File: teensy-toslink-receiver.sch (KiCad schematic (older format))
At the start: 11 parts, among them J1 Conn_01x03, J2 Conn_01x05, J3 Conn_01x05, J4 Conn_01x05, J5 Conn_01x03, J6 Conn_01x04, J7 HDMI_A_1.4, U1 PLR135-T10

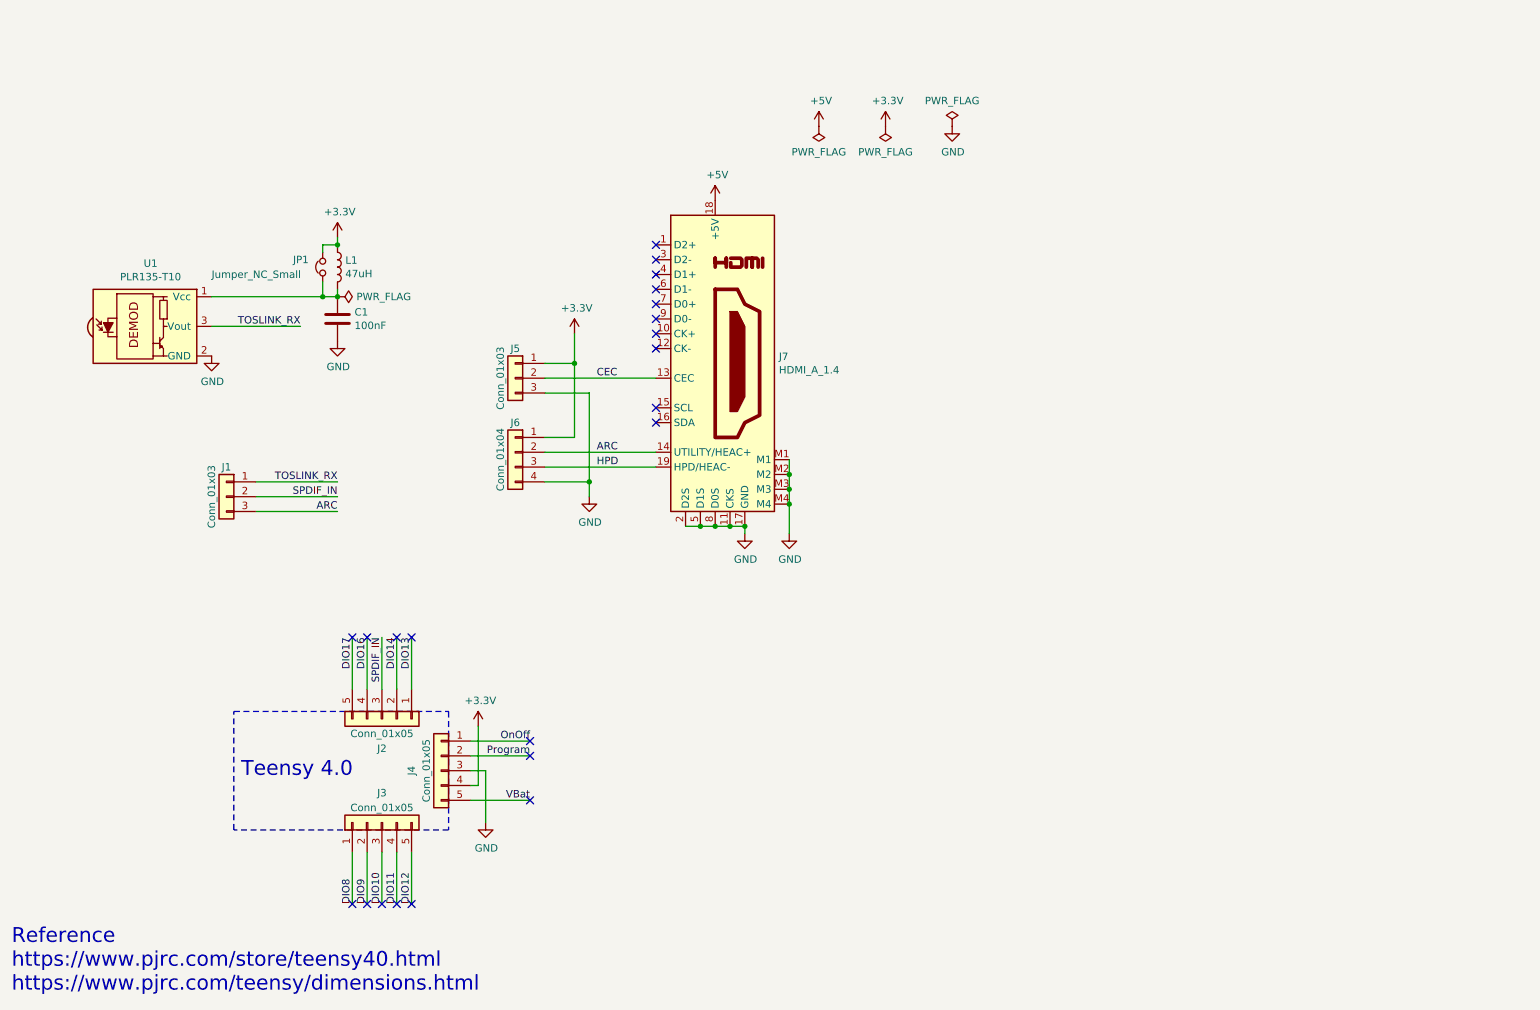
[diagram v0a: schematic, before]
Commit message: schematic: Add HPD and CEC FETs
* N-Channel MOSFET to pull HPD low on connection.
* N-Channel MOSFET acting as a diode to prevent dragging bus down.
* N-Channel MOSFET to detect when HDMI cable is plugged in and 5V is
  available to start operation.
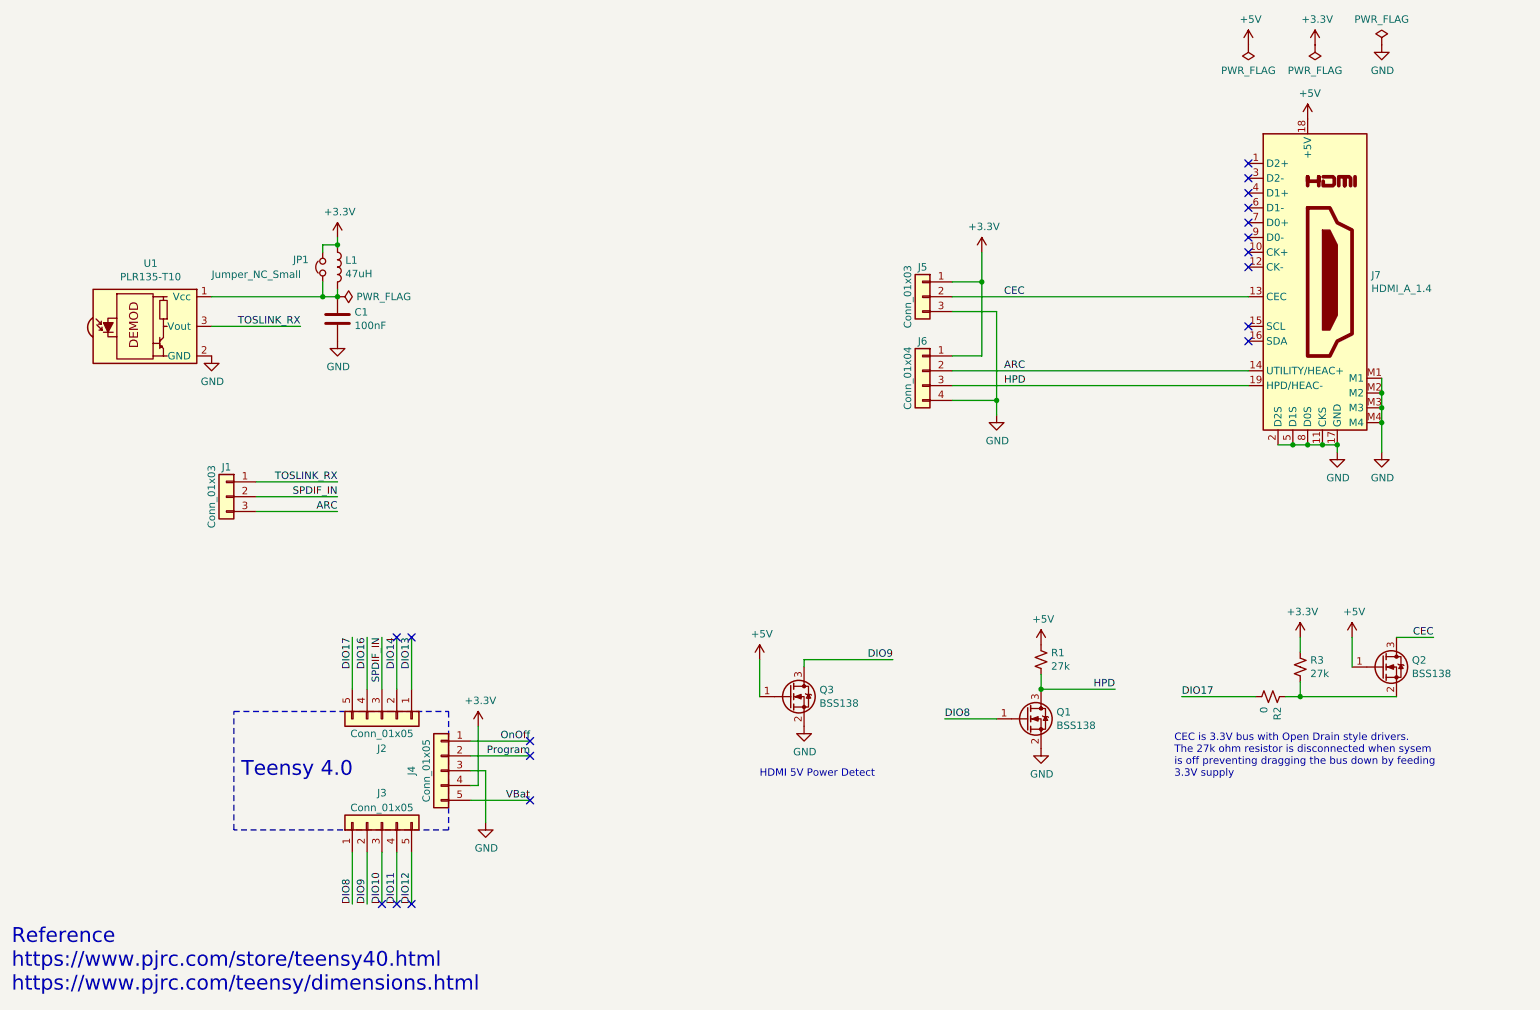
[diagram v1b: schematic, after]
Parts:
- added Q1, Q2, Q3: BSS138, Package_TO_SOT_SMD:SOT-23, symbol Transistor_FET:BSS138
- added R1, R3: 27k, Resistor_SMD:R_0201_0603Metric, symbol Device:R_Small_US
- added R2: 0, Resistor_SMD:R_0201_0603Metric, symbol Device:R_Small_US
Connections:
- net +3V3: now also R3.2
- net +5V: now also Q2.1 (G), Q3.1 (G), R1.1
- net CEC: now also Q2.3 (D)
- net DIO17: now also R2.2
- net DIO8: now also Q1.1 (G)
- net DIO9: now also Q3.3 (D)
- net GND: now also Q1.2 (S), Q3.2 (S)
- net HPD: now also Q1.3 (D), R1.2
- new net: Q2.2 (S), R2.1, R3.1
- no-connect marks 22 -> 18
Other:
- note added: "CEC is 3.3V bus with Open Drain style drivers. \nThe 27k ohm resistor is disconnected when sysem\nis off preventing dragging the bus down by feeding\n3.3V supply"
- note added: "HDMI 5V Power Detect"
- moved on the sheet: J5, J6, J7
